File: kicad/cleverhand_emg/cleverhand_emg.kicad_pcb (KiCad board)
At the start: 4 copper layers, 33 x 16 mm, 24 parts, among them J1 COM_IN, J2 COM_OUT, U1 MCP3564RT-ENC, U2 SN74LVC86ARGYR, U4 SN74ALVC08RGYR, U5 SN74LVC1G132DCKR

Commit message: finished v3
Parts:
- added C3: 10uF, Capacitor_SMD:C_0402_1005Metric, F.Cu at (172.0, 98.6)
- JP1: value SolderJumper_3_Bridged12 -> 1-4_neo_bridge
- U5: value SN74LVC1G132DCKR -> DCK5
- moved D1 3.95 mm to (142.9, 101.0)
- moved D2 3.95 mm to (152.0, 101.0)
- moved D3 3.95 mm to (163.2, 101.0)
- moved G*** 3.95 mm to (166.9, 106.0)
- moved J2 3.95 mm to (161.7, 94.7)
- moved R1 3.95 mm to (166.0, 103.0)
- moved R2 3.95 mm to (165.4, 101.5)
- moved R3 3.95 mm to (165.4, 100.5)
- moved R4 3.95 mm to (165.4, 99.5)
- moved R5 3.95 mm to (165.4, 98.5)
- moved U1 3.95 mm to (168.5, 99.1)
- moved U4 3.95 mm to (145.4, 105.6)
- moved kibuzzard-635971E5 3.95 mm to (157.5, 101.0)
- moved kibuzzard-63597494 3.95 mm to (169.7, 95.8)
- moved C1 3.95 mm to (170.0, 102.2)
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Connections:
- D2 pad 1: Net-(D1-Pad3) -> Net-(D2-Pad1)
- JP1 pad 1: unconnected-(JP1-Pad1) -> Net-(D2-Pad1)
- JP1 pad 2: unconnected-(JP1-Pad2) -> Net-(D1-Pad3)
- JP1 pad 3: unconnected-(JP1-Pad3) -> /NEO_OUT
- U1 pad 1: unconnected-(U1-Pad1) -> /CH_REF
- U1 pad 2: unconnected-(U1-Pad2) -> Net-(U1-Pad2)
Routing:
- net /CH_REF: track 11.2 -> 24.4 mm, vias 0 -> 2
- net /NEO_OUT: track 22.8 -> 34.8 mm, vias 2 -> 3
- net GND: track 18.4 -> 29.3 mm, vias 10 -> 24
- net Net-(J1-Pad15): track 0.00 -> 10.3 mm
- net Net-(J1-Pad14): track 0.00 -> 10.3 mm
- net GNDA: track 27.3 -> 35.9 mm
- net Net-(D1-Pad3): track 18.7 -> 13.4 mm
- net Net-(D2-Pad1): track 0.00 -> 3.48 mm
- net Net-(D3-Pad3): track 15.1 -> 18.2 mm
- net /carry2: track 19.7 -> 22.5 mm
- net +3.3V: track 79.9 -> 77.3 mm
- net /NEO_IN: track 19.1 -> 16.8 mm
- net Net-(U1-Pad2): track 0.00 -> 2.01 mm
- net /S3: track 9.19 -> 11.0 mm
- net /A3: track 14.3 -> 15.6 mm
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- added copper zone on F.Cu, net GND
- added copper zone on In2.Cu, net GND

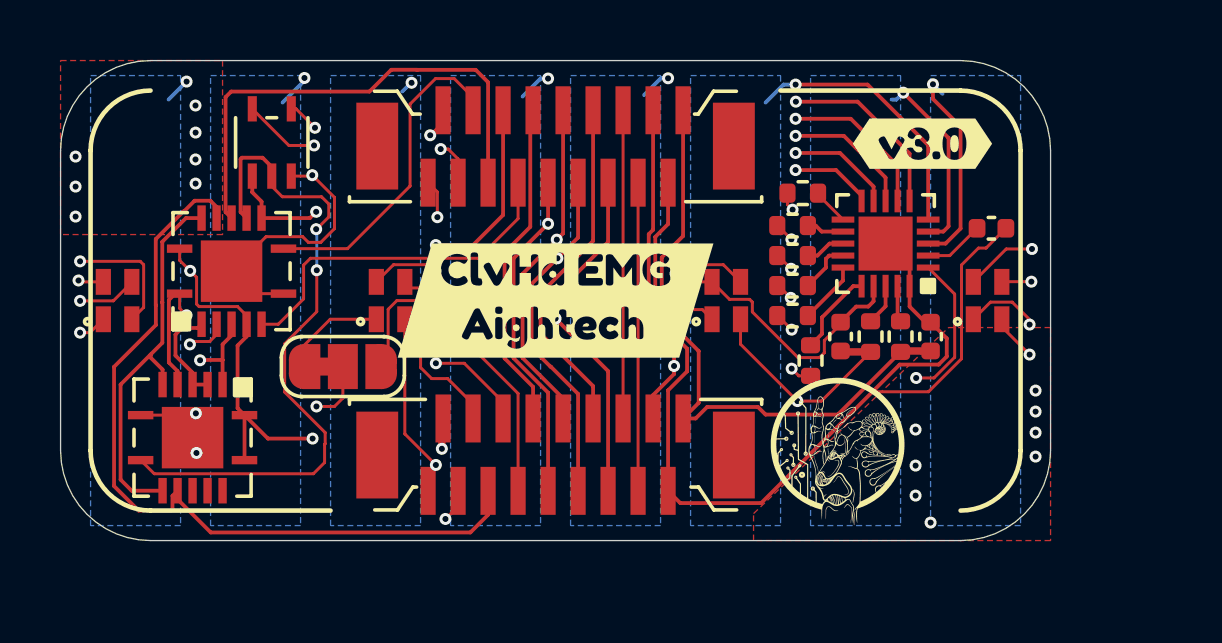
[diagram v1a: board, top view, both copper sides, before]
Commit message: fixed some panel bug for jlcpcb
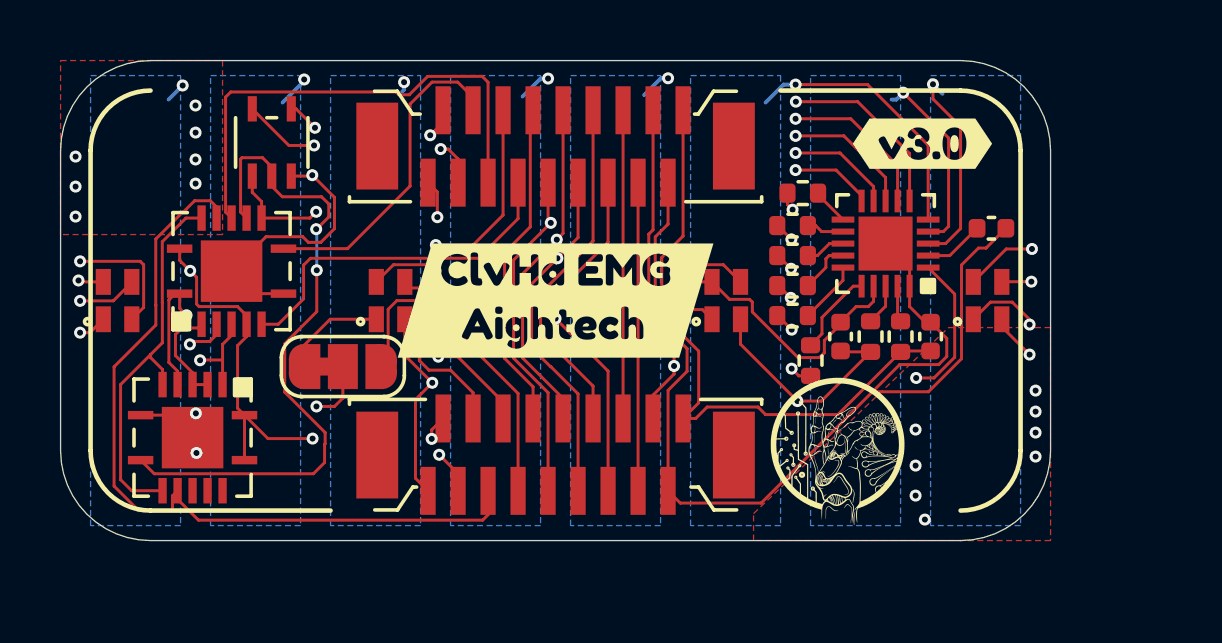
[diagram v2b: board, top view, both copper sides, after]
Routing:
- net /NEO_IN: track 16.8 -> 17.9 mm
- net /A3: track 15.6 -> 16.2 mm

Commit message: v3.1 fixed solder and paste mask and some via pos
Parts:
- removed kibuzzard-635971E5: G***, kibuzzard-635971E5
- removed kibuzzard-63597494: G***, kibuzzard-63597494
- added TP1: TestPoint_Probe, TestPoint:TestPoint_Pad_D1.0mm, F.Cu at (155.0, 101.0)
- added TP2: TestPoint_Probe, TestPoint:TestPoint_Pad_D1.0mm, F.Cu at (158.5, 101.0)
- added TP3: TestPoint_Probe, TestPoint:TestPoint_Pad_D1.0mm, F.Cu at (160.0, 102.0)
- added TP4: TestPoint_Probe, TestPoint:TestPoint_Pad_D1.0mm, F.Cu at (163.5, 99.0)
- added kibuzzard-6360EE7B: G***, kibuzzard-6360EE7B, F.Cu at (157.8, 99.2)
- added kibuzzard-6360EEA9: G***, kibuzzard-6360EEA9, F.Cu at (156.1, 103.1)
- added kibuzzard-6360F8A7: G***, kibuzzard-6360F8A7, F.Cu at (169.7, 95.8)
- U5: value DCK5 -> SN74LVC1G132DCKR
- moved D1 0.30 mm to (143.2, 101.0)
- moved U2 0.16 mm to (146.9, 100.0)
- moved D4 0.10 mm to (171.8, 101.0)
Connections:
- net Net-(J1-Pad14) renamed /AUX2
- net Net-(J1-Pad15) renamed /AUX3
- net Net-(J1-Pad8) renamed /AUX1
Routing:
- net /cs_adc: track 19.0 -> 21.4 mm
- net GND: track 29.1 -> 30.6 mm
- net /AUX2: track 10.3 -> 11.3 mm
- net +3.3V: track 77.7 -> 78.4 mm
- net /AUX1: track 11.1 -> 11.7 mm
